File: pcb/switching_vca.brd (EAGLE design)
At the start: 100 x 22 mm, 37 parts, among them Q101 PMOS, Q102 NJFET, U101 LM319, U102 LF353D, U103 LF353D, U701 V_REG_LDOSMD

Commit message: Routed the board with a travesty of VIAs
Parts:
- added TP101: (no value), SparkFun:1X01
- added U$1: (no value), SparkFun:OSHW-LOGO-L
- moved C106 40.7 mm to (8.89, 11.4), turned to 180 degrees
- moved C104 38.1 mm to (11.4, 21.6), turned to 180 degrees
- moved R110 37.2 mm to (12.7, 11.4), turned to 0 degrees
- moved R303 36.9 mm to (45.7, 14.0), turned to 90 degrees
- moved U103 32.2 mm to (12.7, 16.5), turned to 180 degrees
- moved C603 32.2 mm to (8.89, 16.5), turned to 270 degrees
- moved R111 29.9 mm to (16.5, 8.89), turned to 90 degrees
- moved C103 29.6 mm to (15.2, 21.6), turned to 0 degrees
- moved C601 29.3 mm to (38.1, 6.35), turned to 90 degrees
- moved U102 28.5 mm to (41.9, 6.35), turned to 0 degrees
- moved C105 27.7 mm to (17.8, 11.4), turned to 0 degrees
- moved R108 27.7 mm to (19.3, 19.1), turned to 90 degrees
- moved R304 25.4 mm to (41.9, 11.4), turned to 0 degrees
- moved R301 23.4 mm to (43.2, 14.0), turned to 90 degrees
- moved R109 22.9 mm to (17.8, 15.2), turned to 90 degrees
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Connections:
- net IN: now also JP1.8; no longer JP1.3
- net N$15: now also TP101.1
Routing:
- net N$7: track 5.00 -> 50.4 mm, vias 0 -> 4
- net N$6: track 51.5 -> 11.9 mm
- net +12V: track 120.1 -> 80.6 mm
- net IN: track 12.4 -> 43.1 mm, vias 0 -> 1
- net 5V3: track 4.71 -> 32.3 mm, vias 0 -> 2
- net N$15: track 38.6 -> 12.1 mm, vias 2 -> 1
- net +5V: track 35.9 -> 61.4 mm, vias 1 -> 2
- net -12V: track 58.6 -> 78.3 mm, vias 3 -> 1
- net INT: track 16.0 -> 28.3 mm, vias 0 -> 2
- net N$8: track 5.81 -> 12.4 mm
- net N$4: track 12.2 -> 6.06 mm
- net N$: track 19.1 -> 24.9 mm, vias 0 -> 2
- net N$11: track 13.5 -> 18.7 mm
- net R301: track 11.2 -> 6.97 mm
- net N$3: track 11.4 -> 7.83 mm, vias 2 -> 0
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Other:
- board size 100 x 22 mm -> 48 x 23 mm
- board text added: "Digitally Controlled Amplifier Alpha"

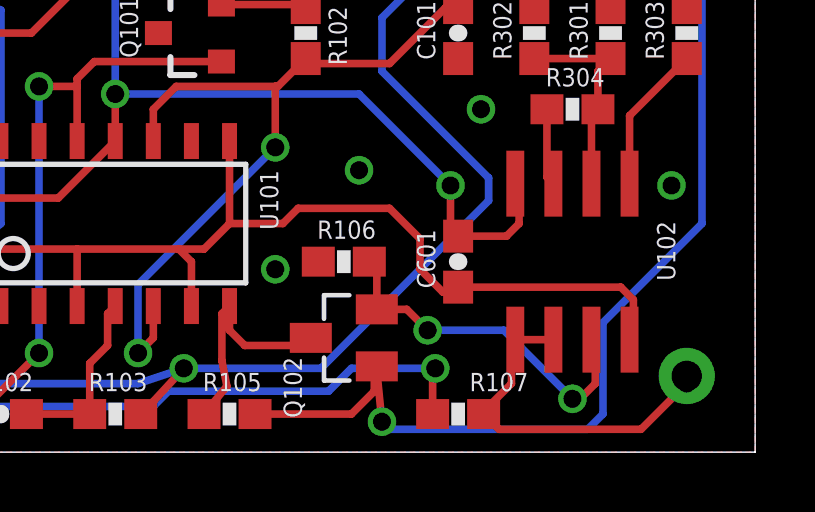
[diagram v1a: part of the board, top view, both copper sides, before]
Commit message: added test point for PWM comparator output
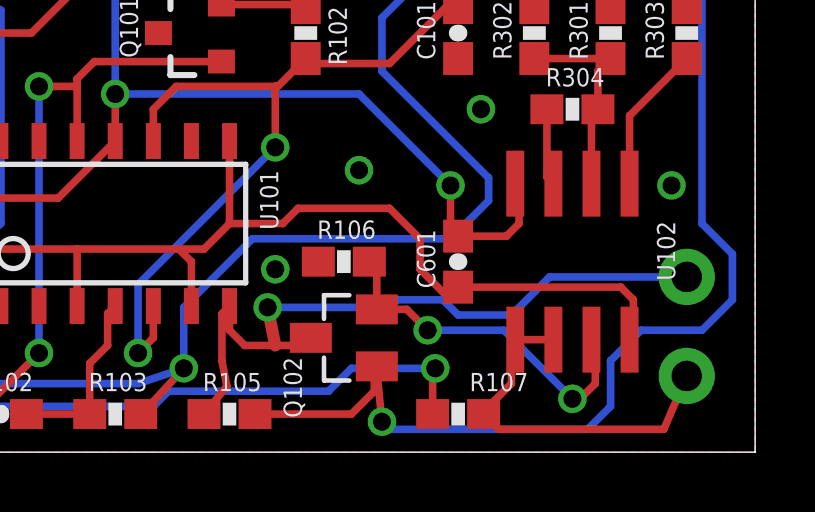
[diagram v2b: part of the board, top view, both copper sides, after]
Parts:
- added TP102: (no value), SparkFun:1X01
- moved TP101 3.30 mm to (45.7, 5.84)
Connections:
- net N$15: now also TP102.1; no longer TP101.1
- net N$3: now also TP101.1
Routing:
- net N$3: track 7.83 -> 23.9 mm, vias 0 -> 1
- net IN: track 43.1 -> 45.1 mm
- net +5V: track 61.4 -> 62.6 mm
- net N$15: track 12.1 -> 12.3 mm, vias 1 -> 0
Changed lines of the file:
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@@
 <layer number="109" name="fp9" color="7" fill="1" visible="no" active="yes"/>
 <layer number="110" name="fp0" color="7" fill="1" visible="no" active="yes"/>
-<layer number="111" name="LPC17xx" color="7" fill="1" visible="yes" active="yes"/>
+<layer number="111" name="LPC17xx" color="7" fill="1" visible="no" active="yes"/>
 <layer number="116" name="Patch_BOT" color="9" fill="4" visible="no" active="yes"/>
 <layer number="121" name="_tsilk" color="7" fill="1" visible="no" active="yes"/>
@@
 <layer number="144" name="Drill_legend" color="7" fill="1" visible="no" active="yes"/>
 <layer number="151" name="HeatSink" color="7" fill="1" visible="no" active="yes"/>
-<layer number="199" name="Contour" color="7" fill="1" visible="yes" active="yes"/>
+<layer number="199" name="Contour" color="7" fill="1" visible="no" active="yes"/>
 <layer number="200" name="200bmp" color="1" fill="10" visible="no" active="yes"/>
 <layer number="201" name="201bmp" color="2" fill="10" visible="no" active="yes"/>
@@
 <attribute name="VALUE" x="30.988" y="7.112" size="1.016" layer="27" rot="R180"/>
 </element>
-<element name="TP101" library="SparkFun" package="1X01" value="" x="45.72" y="2.54" smashed="yes" rot="MR0">
-<attribute name="NAME" x="46.3042" y="4.3688" size="0.6096" layer="26" rot="MR0"/>
+<element name="TP102" library="SparkFun" package="1X01" value="" x="45.72" y="2.54" smashed="yes" rot="MR0">
+<attribute name="NAME" x="47.0662" y="0.3048" size="0.6096" layer="26" rot="MR0"/>
 <attribute name="VALUE" x="46.99" y="-0.635" size="1.27" layer="28" rot="MR0"/>
 </element>
 <element name="U$1" library="SparkFun" package="OSHW-LOGO-L" value="" x="27.686" y="5.588" rot="MR0"/>
+<element name="TP101" library="SparkFun" package="1X01" value="" x="45.72" y="5.842" smashed="yes" rot="MR0">
+<attribute name="NAME" x="47.0662" y="7.6708" size="0.6096" layer="26" rot="MR0"/>
+<attribute name="VALUE" x="46.99" y="2.667" size="1.27" layer="28" rot="MR0"/>
+</element>
 </elements>
 <signals>
@@
 <wire x1="28.956" y1="2.794" x2="27.94" y2="1.69" width="0.254" layer="1"/>
 <wire x1="27.94" y1="1.69" x2="27.52" y2="1.27" width="0.254" layer="1"/>
-<wire x1="28.956" y1="2.794" x2="33.528" y2="2.794" width="0.254" layer="16"/>
-<wire x1="33.528" y1="2.794" x2="39.116" y2="8.382" width="0.254" layer="16"/>
 <wire x1="45.72" y1="17.018" x2="45.72" y2="18.542" width="0.254" layer="16"/>
 <wire x1="45.72" y1="18.542" x2="43.942" y2="20.32" width="0.254" layer="16"/>
@@
 <wire x1="36.83" y1="15.748" x2="44.45" y2="15.748" width="0.254" layer="16"/>
 <wire x1="44.45" y1="15.748" x2="45.72" y2="17.018" width="0.254" layer="16"/>
+<wire x1="28.956" y1="2.794" x2="28.956" y2="4.826" width="0.254" layer="16"/>
+<wire x1="28.956" y1="4.826" x2="31.242" y2="7.112" width="0.254" layer="16"/>
+<wire x1="31.242" y1="7.112" x2="37.846" y2="7.112" width="0.254" layer="16"/>
+<wire x1="37.846" y1="7.112" x2="39.116" y2="8.382" width="0.254" layer="16"/>
 </signal>
 <signal name="N$4">
@@
 <wire x1="30.48" y1="4.87" x2="30.48" y2="4.064" width="0.254" layer="1"/>
 <wire x1="30.48" y1="4.064" x2="30.988" y2="3.556" width="0.254" layer="1"/>
-<wire x1="30.988" y1="3.556" x2="32.936" y2="3.556" width="0.254" layer="1"/>
+<wire x1="30.988" y1="3.556" x2="32.004" y2="3.556" width="0.254" layer="1"/>
+<wire x1="32.004" y1="3.556" x2="32.936" y2="3.556" width="0.254" layer="1"/>
 <wire x1="32.936" y1="3.556" x2="33.19" y2="3.81" width="0.254" layer="1"/>
+<contactref element="TP101" pad="1"/>
+<wire x1="35.814" y1="4.826" x2="31.75" y2="4.826" width="0.254" layer="16"/>
+<via x="31.75" y="4.826" extent="1-16" drill="0.6" shape="square"/>
+<wire x1="31.75" y1="4.826" x2="32.004" y2="3.556" width="0.4064" layer="1"/>
+<wire x1="45.72" y1="5.842" x2="41.148" y2="5.842" width="0.254" layer="16"/>
+<wire x1="41.148" y1="5.842" x2="39.878" y2="4.572" width="0.254" layer="16"/>
+<wire x1="39.878" y1="4.572" x2="38.1" y2="4.572" width="0.254" layer="16"/>
+<wire x1="38.1" y1="4.572" x2="37.592" y2="5.08" width="0.254" layer="16"/>
+<wire x1="37.592" y1="5.08" x2="36.068" y2="5.08" width="0.254" layer="16"/>
+<wire x1="36.068" y1="5.08" x2="35.814" y2="4.826" width="0.254" layer="16"/>
 </signal>
 <signal name="N$6">
@@
 <wire x1="40.64" y1="21.844" x2="40.64" y2="20.32" width="0.254" layer="16"/>
 <wire x1="46.228" y1="17.018" x2="46.228" y2="7.62" width="0.254" layer="16"/>
-<wire x1="46.228" y1="7.62" x2="42.926" y2="4.318" width="0.254" layer="16"/>
-<wire x1="42.926" y1="4.318" x2="42.926" y2="1.27" width="0.254" layer="16"/>
-<wire x1="42.926" y1="1.27" x2="42.418" y2="0.762" width="0.254" layer="16"/>
 <wire x1="42.418" y1="0.762" x2="35.814" y2="0.762" width="0.254" layer="16"/>
 <wire x1="35.814" y1="0.762" x2="35.56" y2="1.016" width="0.254" layer="16"/>
+<wire x1="42.418" y1="0.762" x2="43.18" y2="1.524" width="0.254" layer="16"/>
+<wire x1="43.18" y1="1.524" x2="43.18" y2="3.048" width="0.254" layer="16"/>
+<wire x1="43.18" y1="3.048" x2="44.196" y2="4.064" width="0.254" layer="16"/>
+<wire x1="44.196" y1="4.064" x2="46.228" y2="4.064" width="0.254" layer="16"/>
+<wire x1="46.228" y1="4.064" x2="47.244" y2="5.08" width="0.254" layer="16"/>
+<wire x1="47.244" y1="5.08" x2="47.244" y2="6.604" width="0.254" layer="16"/>
+<wire x1="47.244" y1="6.604" x2="46.228" y2="7.62" width="0.254" layer="16"/>
 </signal>
 <signal name="OUT">
@@
 <wire x1="39.878" y1="3.623" x2="40.005" y2="3.75" width="0.254" layer="1"/>
 <wire x1="40.005" y1="3.75" x2="41.275" y2="3.75" width="0.254" layer="1"/>
-<contactref element="TP101" pad="1"/>
-<wire x1="45.72" y1="2.54" x2="45.72" y2="2.286" width="0.254" layer="16"/>
-<wire x1="45.72" y1="2.286" x2="44.196" y2="0.762" width="0.254" layer="1"/>
-<wire x1="44.196" y1="0.762" x2="39.458" y2="0.762" width="0.254" layer="1"/>
+<contactref element="TP102" pad="1"/>
+<wire x1="45.72" y1="2.54" x2="44.958" y2="0.762" width="0.254" layer="1"/>
+<wire x1="44.958" y1="0.762" x2="39.458" y2="0.762" width="0.254" layer="1"/>
 <wire x1="39.458" y1="0.762" x2="38.95" y2="1.27" width="0.254" layer="1"/>
-<via x="45.72" y="2.286" extent="1-16" drill="0.6" shape="square"/>
 </signal>
 <signal name="INT">
